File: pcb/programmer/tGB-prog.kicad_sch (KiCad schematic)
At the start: 40 parts, among them J1 ZX62R-B-5P, J2 PROG_PORT, U1 FT2232D, U2 93LC56BT-I/OT, U3 TPS79901DDCR, Y1 NX8045GB-6MHZ-STD-CSF-3

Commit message: set title and revision
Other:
- title: (none) -> tsuraraGB Programmer PCB
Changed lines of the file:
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@@
 (kicad_sch (version 20211123) (generator eeschema)
   (paper "A4")
+  (title_block
+    (title "tsuraraGB Programmer PCB")
+    (rev "A")
+  )
   (junction (at 167.64 101.6) (diameter 0) (color 0 0 0 0)
   )

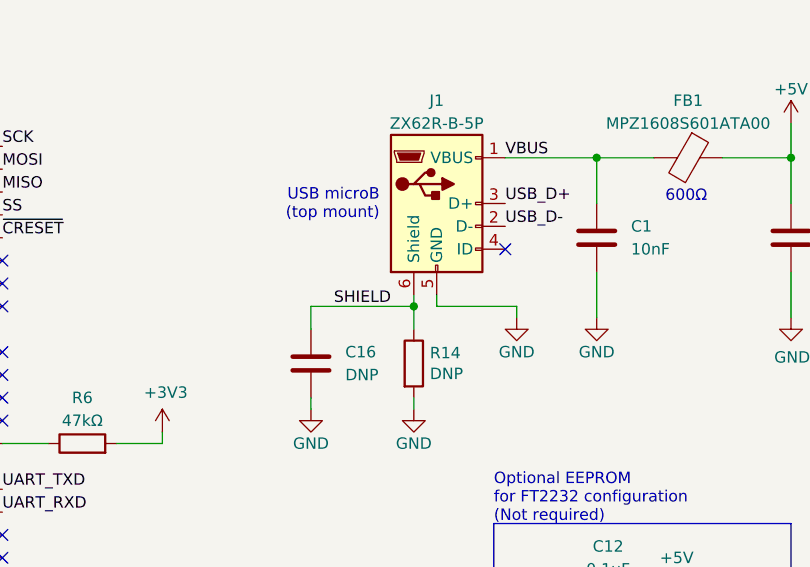
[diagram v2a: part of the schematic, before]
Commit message: migrate KiCad 7 -> 10
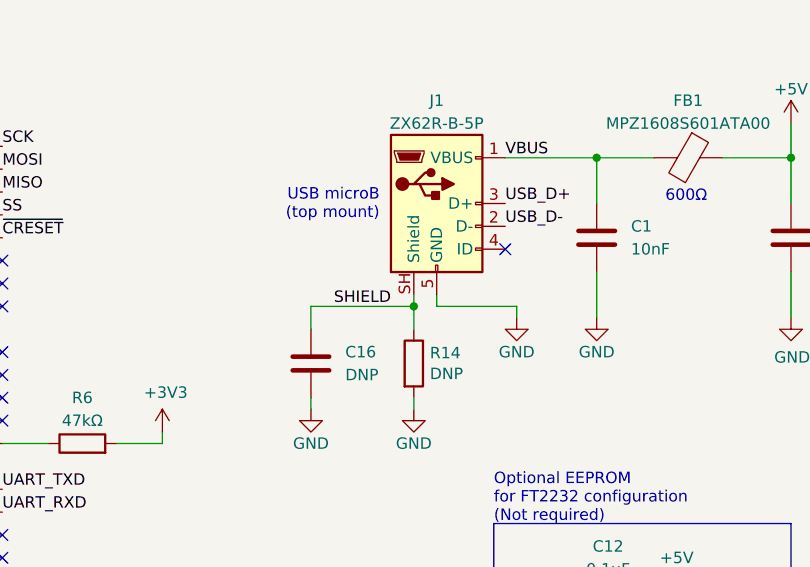
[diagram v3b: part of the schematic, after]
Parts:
- D1: footprint LED_Addition:LED_0603_1608Metric_Castellated -> ProjectSpecific:LED_0603_1608Metric_Castellated
- J1: footprint ZX62R-B-5P:ZX62R-B-5P -> ProjectSpecific:ZX62R-B-5P
- J2: footprint Pin_Sidemount:PinSocket_1x10_P2.54_Sidemount -> ProjectSpecific:PinSocket_1x10_P2.54_Sidemount
- U3: symbol TPS79901DDCR:TPS79901DDCR -> ProjectSpecific:TPS79901DDCR
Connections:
- net SHIELD: now also J1.SH (Shield); no longer J1.6 (Shield)
